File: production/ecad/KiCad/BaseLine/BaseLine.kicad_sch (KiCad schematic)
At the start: 0 parts

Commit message: Changed footprints again
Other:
- removed sheet IMU
- removed sheet Load Cell
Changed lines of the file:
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@@
-	)
-	(sheet
-		(at 204.47 33.02)
-		(size 62.23 48.26)
-		(fields_autoplaced yes)
-		(stroke
-			(width 0.1524)
-			(type solid)
-		)
-		(fill
-			(color 0 0 0 0.0000)
-		)
-		(property "Sheetname" "Load Cell"
-			(at 204.47 32.3084 0)
-			(effects
-				(font
-					(size 1.27 1.27)
-				)
-				(justify left bottom)
-			)
-		)
-		(property "Sheetfile" "loadcell.kicad_sch"
-			(at 204.47 81.8646 0)
-			(effects
-				(font
-					(size 1.27 1.27)
-				)
-				(justify left top)
-			)
-		)
-		(instances
-			(project "BaseLine"
-				(path "/ba9eda21-3882-41e1-8265-3d8ac781da20"
-					(page "6")
-				)
-			)
-		)
 	)
 	(sheet
@@
 				)
 			)
-		)
-	)
-	(sheet
-		(at 38.1 95.25)
-		(size 50.8 43.18)
-		(fields_autoplaced yes)
-		(stroke
-			(width 0.1524)
-			(type solid)
-		)
-		(fill
-			(color 0 0 0 0.0000)
-		)
-		(property "Sheetname" "IMU"
-			(at 38.1 94.5384 0)
-			(effects
-				(font
-					(size 1.27 1.27)
-				)
-				(justify left bottom)
-			)
-		)
-		(property "Sheetfile" "imu.kicad_sch"
-			(at 38.1 139.0146 0)
-			(effects
-				(font
-					(size 1.27 1.27)
-				)
-				(justify left top)
-			)
-		)
-		(instances
-			(project "BaseLine"
-				(path "/ba9eda21-3882-41e1-8265-3d8ac781da20"
-					(page "4")
-				)
-			)

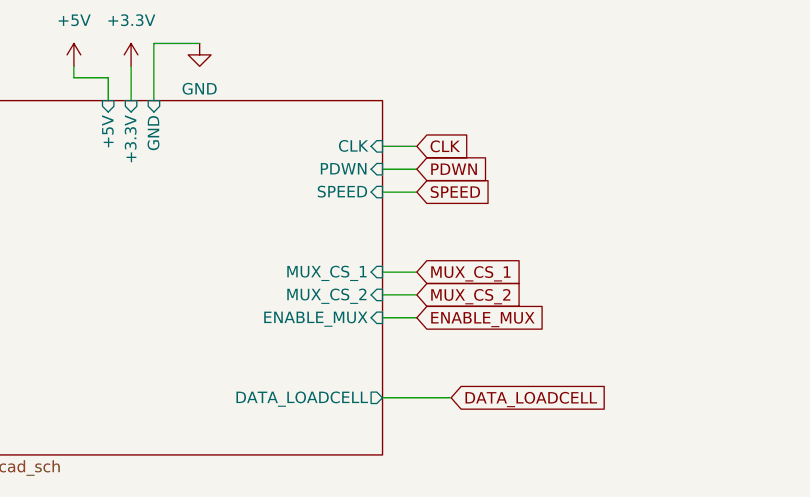
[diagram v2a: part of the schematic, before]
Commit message: Fixed I/O mux select pins
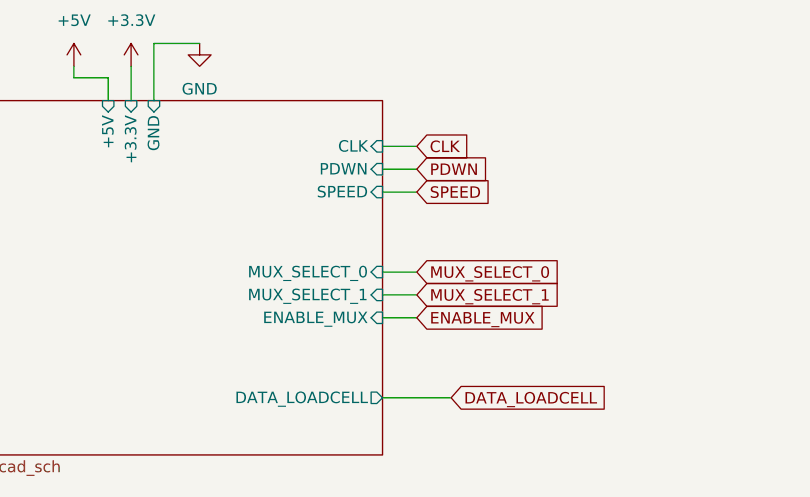
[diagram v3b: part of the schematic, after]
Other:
- sheet IO ports: added MUX_SELECT_0, MUX_SELECT_1; removed MUX_CS_1, MUX_CS_2
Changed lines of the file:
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@@
 		)
 	)
-	(global_label "MUX_CS_1"
+	(global_label "MUX_SELECT_0"
 		(shape input)
 		(at 93.98 171.45 0)
@@
 		)
 		(property "Intersheetrefs" "${INTERSHEET_REFS}"
-			(at 106.5808 171.45 0)
+			(at 110.8745 171.45 0)
 			(effects
 				(font
@@
 		)
 	)
-	(global_label "MUX_CS_2"
+	(global_label "MUX_SELECT_1"
 		(shape input)
 		(at 93.98 173.99 0)
@@
 		)
 		(property "Intersheetrefs" "${INTERSHEET_REFS}"
-			(at 106.5808 173.99 0)
+			(at 110.8745 173.99 0)
 			(effects
 				(font
@@
 			)
 		)
-		(pin "MUX_CS_1" input
+		(pin "MUX_SELECT_0" input
 			(at 90.17 171.45 0)
 			(effects
@@
 			)
 		)
-		(pin "MUX_CS_2" input
+		(pin "MUX_SELECT_1" input
 			(at 90.17 173.99 0)
 			(effects

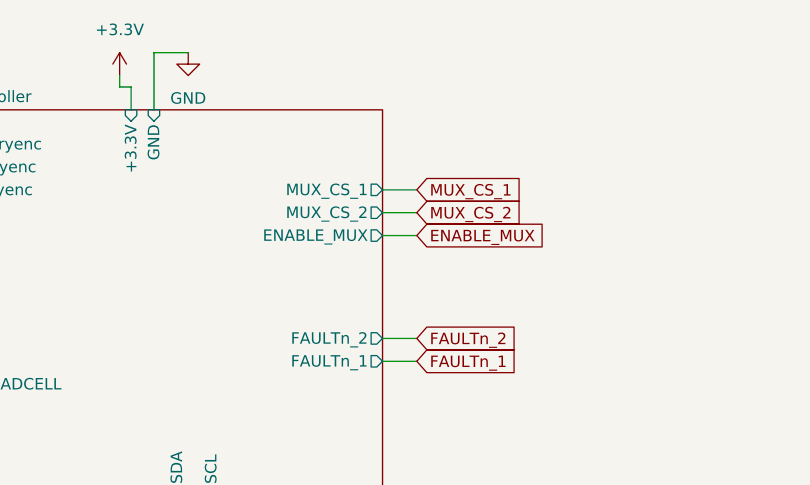
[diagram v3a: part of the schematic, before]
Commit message: Changed MUX chip select names to match Bryan
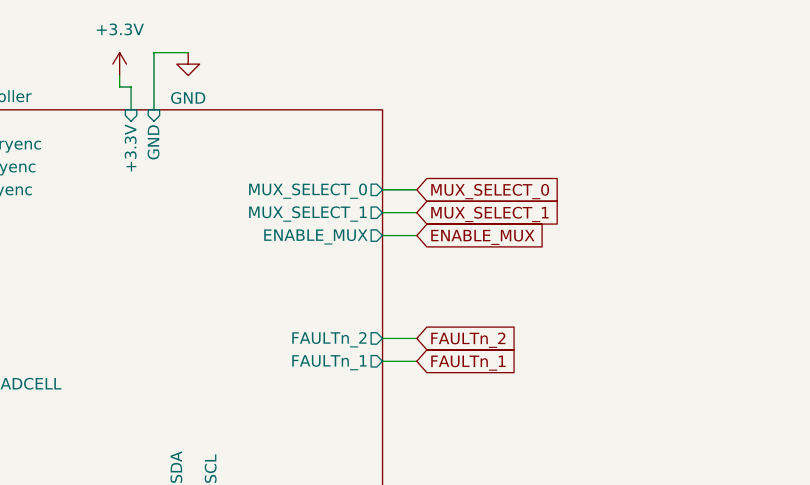
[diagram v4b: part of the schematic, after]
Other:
- sheet Microcontroller ports: added MUX_SELECT_0, MUX_SELECT_1; removed MUX_CS_1, MUX_CS_2
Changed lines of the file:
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@@
 		)
 	)
-	(global_label "MUX_CS_2"
+	(global_label "MUX_SELECT_1"
 		(shape input)
 		(at 184.15 45.72 0)
@@
 		)
 		(property "Intersheetrefs" "${INTERSHEET_REFS}"
-			(at 196.7508 45.72 0)
+			(at 201.0445 45.72 0)
 			(effects
 				(font
@@
 		)
 	)
-	(global_label "MUX_CS_1"
+	(global_label "MUX_SELECT_0"
 		(shape input)
 		(at 184.15 43.18 0)
@@
 		)
 		(property "Intersheetrefs" "${INTERSHEET_REFS}"
-			(at 196.7508 43.18 0)
+			(at 201.0445 43.18 0)
 			(effects
 				(font
@@
 			)
 		)
-		(pin "MUX_CS_2" output
+		(pin "MUX_SELECT_1" output
 			(at 180.34 45.72 0)
 			(effects
@@
 			)
 		)
-		(pin "MUX_CS_1" output
+		(pin "MUX_SELECT_0" output
 			(at 180.34 43.18 0)
 			(effects
